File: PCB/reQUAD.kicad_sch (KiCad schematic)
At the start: 7 parts, among them J1 Model_100_System_BUS, U1 74LVC2G79, U2 74AC02, U4 74AC573, U5 628128

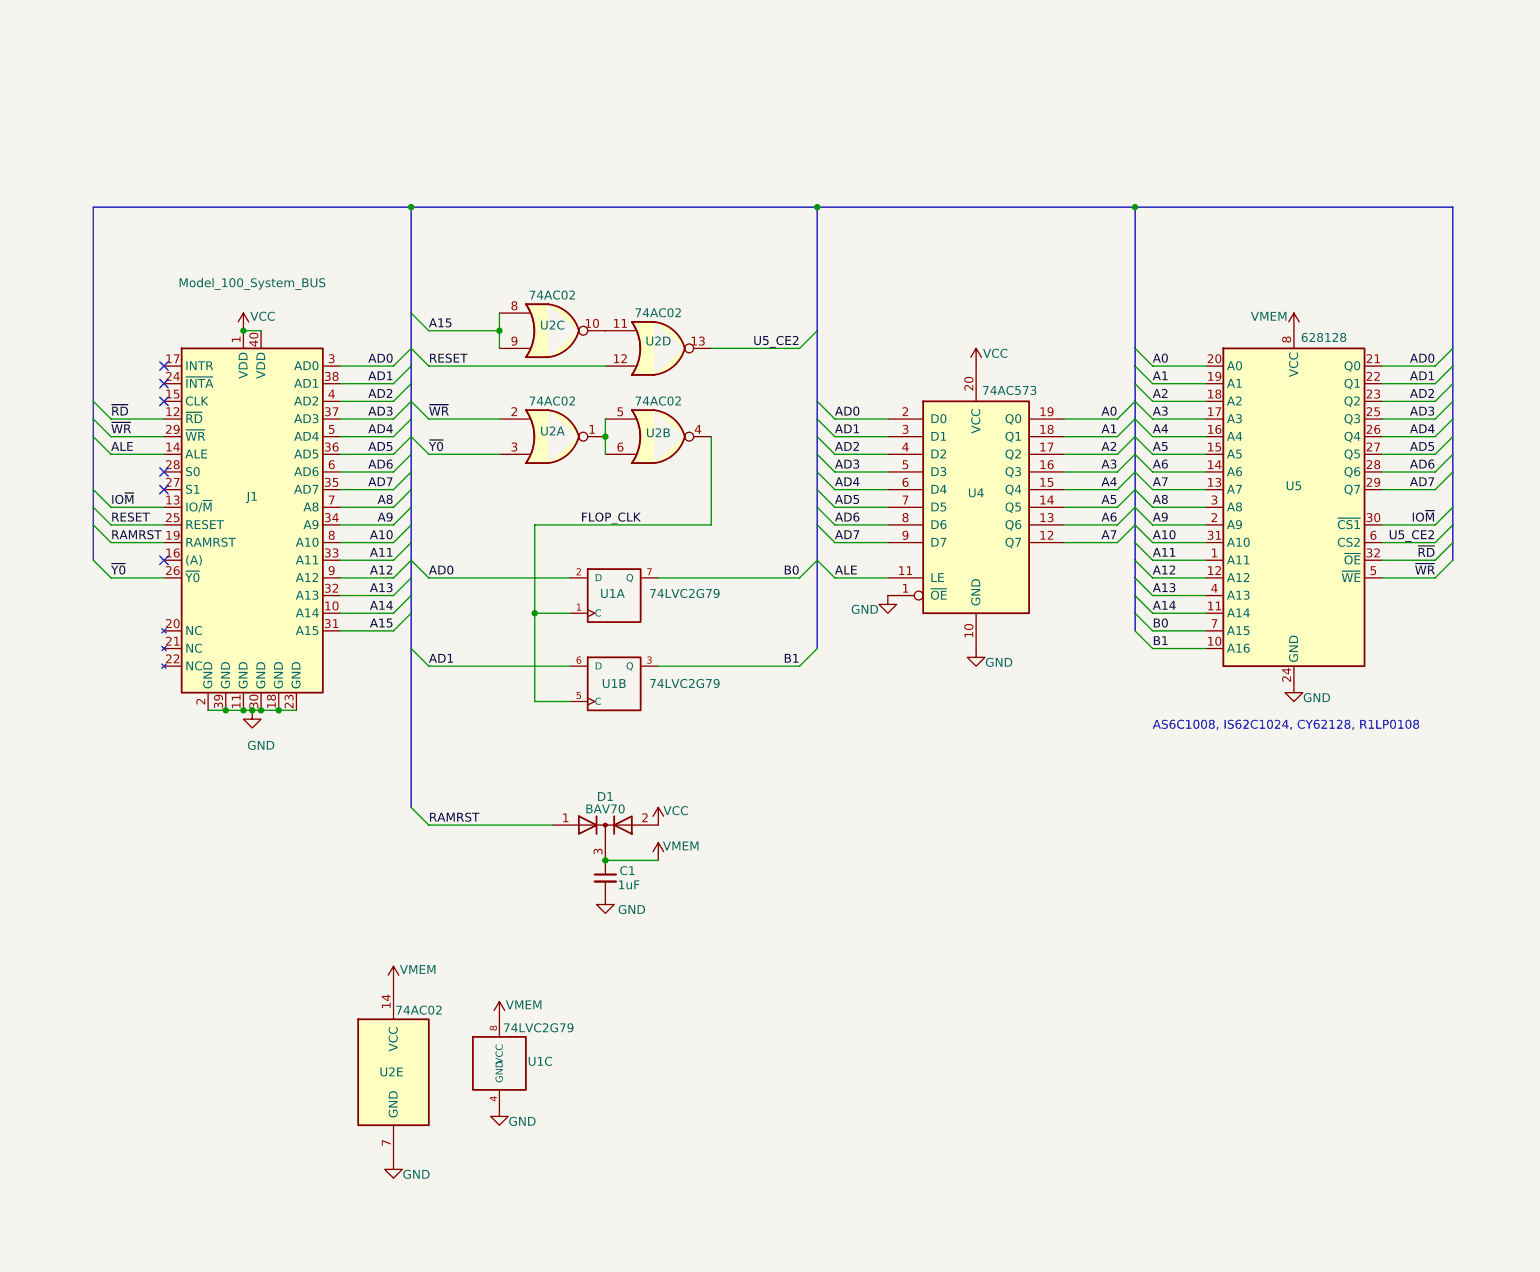
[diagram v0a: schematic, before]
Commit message: Try Steve's new idea: Pull (A)* low instead of pulling RAMRST high
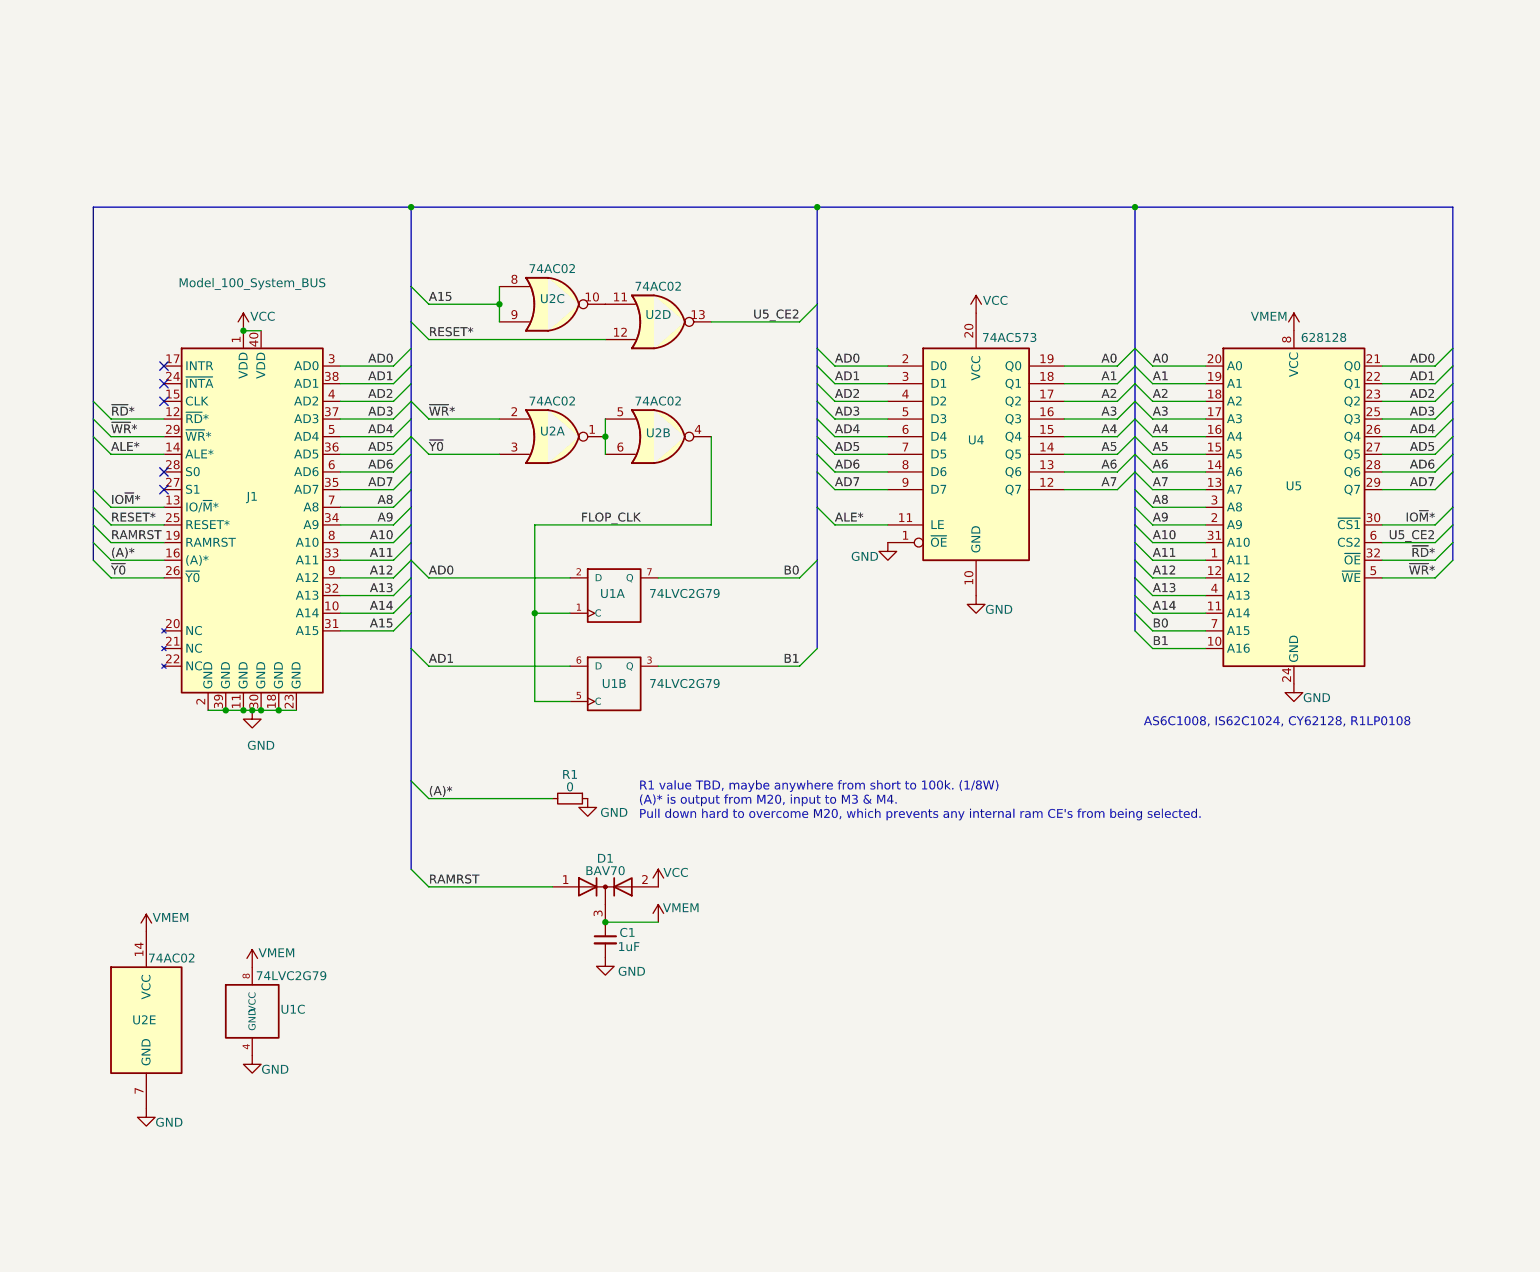
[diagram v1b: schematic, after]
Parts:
- added R1: 0, 000_LOCAL:R_0805, symbol 000_LOCAL:R_Small
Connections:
- net GND: now also R1.1
- net (A)*: now reaches J1.16 ((A)*)
- net (A)*: now also R1.2
- net ALE renamed ALE*
- net IO~{M} renamed IO~{M}*
- net RESET renamed RESET*
- net ~{RD} renamed ~{RD}*
- net ~{WR} renamed ~{WR}*
- no-connect marks 6 -> 5
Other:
- note added: "R1 value TBD, maybe anywhere from short to 100k. (1/8W) (A)* is output from M20, input to M3 & M4. Pull down hard to overcome M20, which prevents any internal ram CE's from being selected."
- moved on the sheet: C1, D1, U1C, U2C, U2D, U2E, U4

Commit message: pcb routing vcc vmem A0-A3
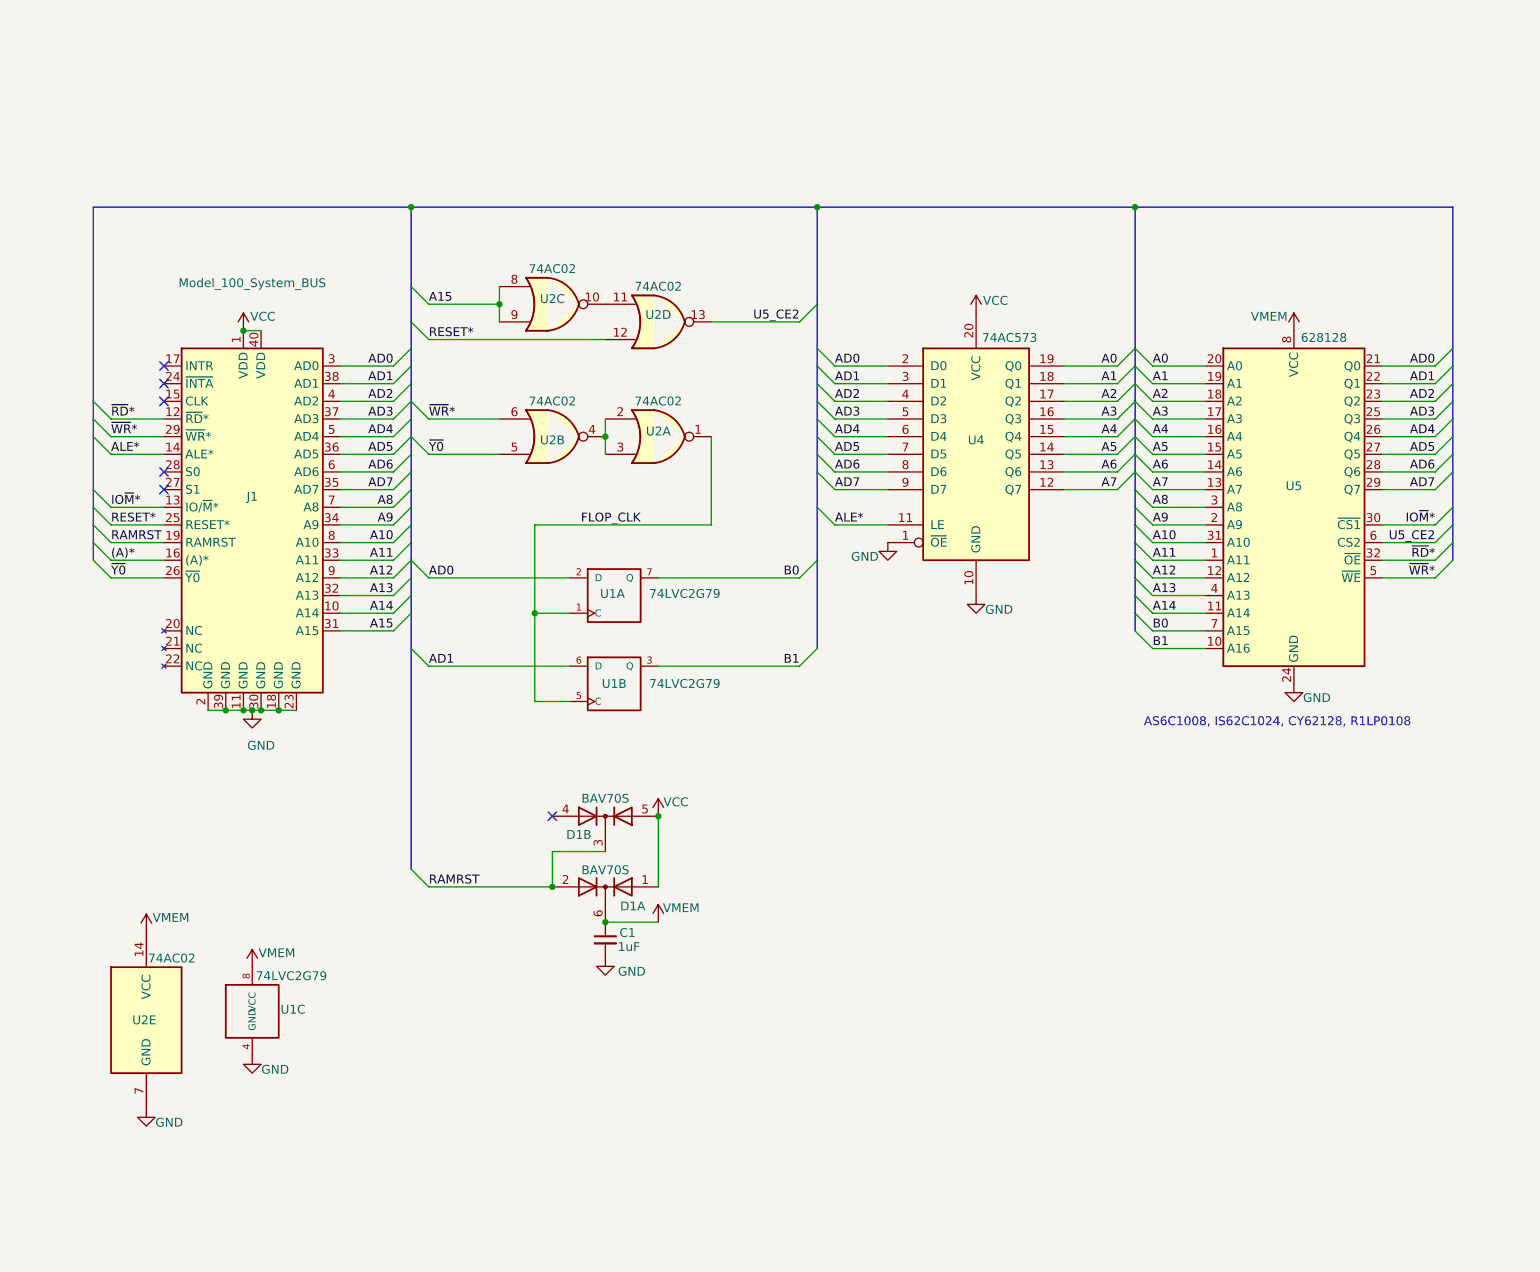
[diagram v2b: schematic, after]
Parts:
- removed D1: BAV70, 000_LOCAL:SOT-23, symbol 000_LOCAL:BAV70
- removed R1: 0, 000_LOCAL:R_0805, symbol 000_LOCAL:R_Small
- added D1: BAV70S, 000_LOCAL:SOT-363_symmetric, symbol 000_LOCAL:BAV70S
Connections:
- net FLOP_CLK: now also U2.1; no longer U2.4
- net RAMRST: now also D1.2 (A), D1.3 (K)
- net VCC: now also D1.1 (A), D1.5 (A)
- net VMEM: now also D1.6 (K)
- net ~{WR}*: now also U2.6; no longer U2.2
- net ~{Y0}: now also U2.5; no longer U2.3
- new net: U2.2, U2.3, U2.4
- no-connect marks 5 -> 6
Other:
- note removed: "R1 value TBD, maybe anywhere from short to 100k. (1/8W) (A)* is output from M20, input to M3 & M4. Pull down hard to overcome M20, which prevents any internal ram CE's from being selected."
- moved on the sheet: U2A, U2B

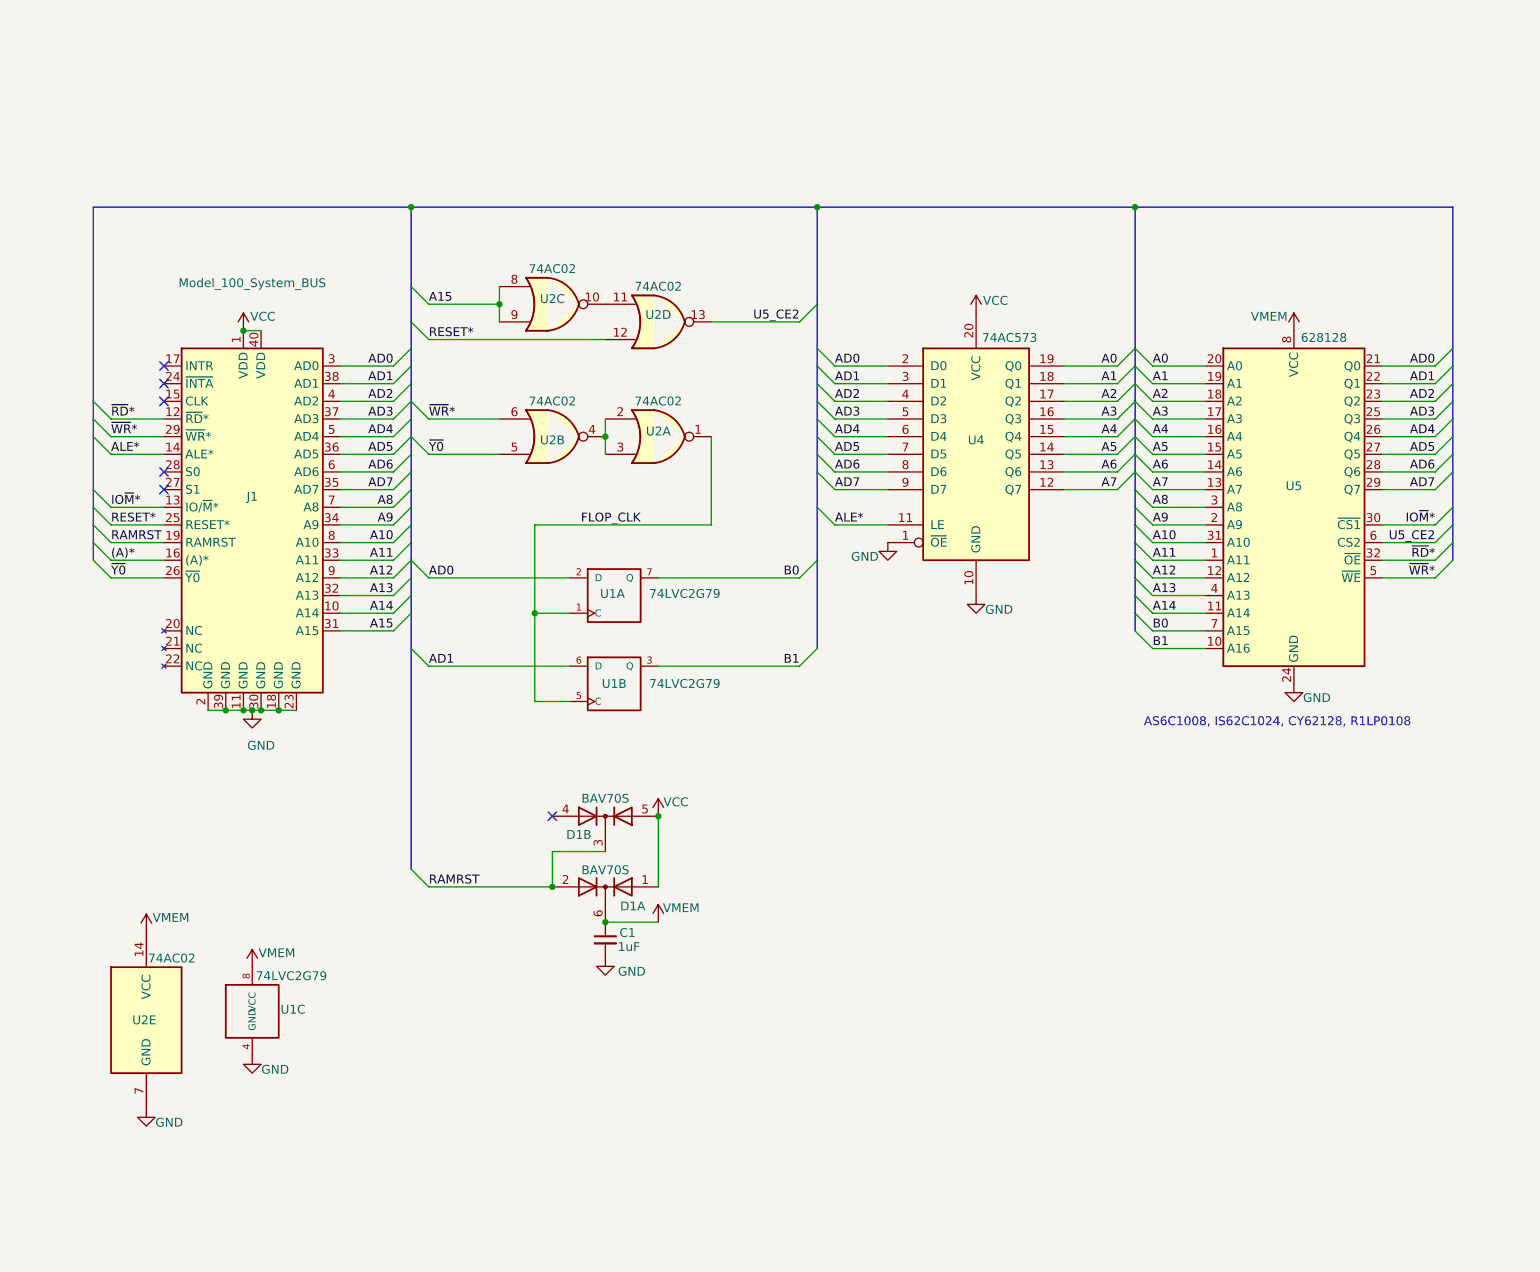
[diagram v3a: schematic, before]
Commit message: only need the flipflops on vmem?
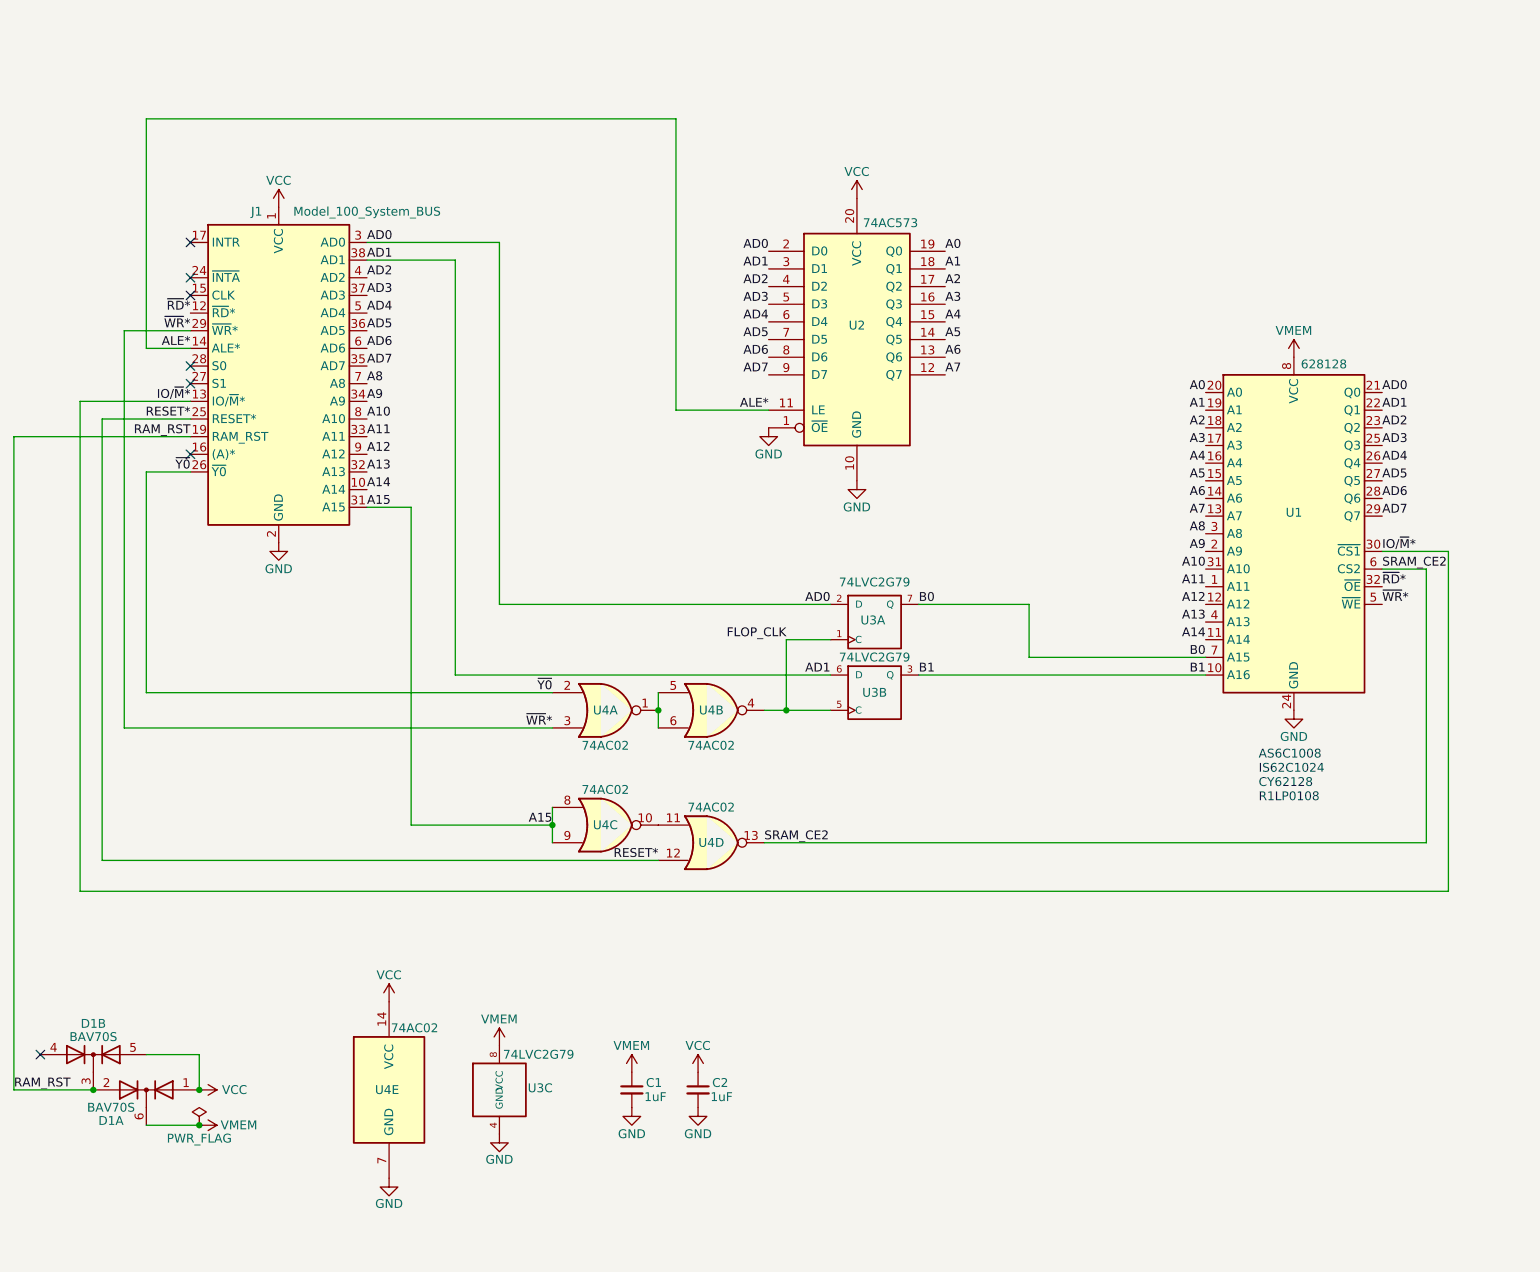
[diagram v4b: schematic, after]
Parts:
- added C2: 1uF, 000_LOCAL:C_0805, symbol 000_LOCAL:C_Small
- J1: footprint 000_LOCAL:DIP-40_pins -> Package_DIP:DIP-40_W15.24mm_Socket
- renumbered U5 to U1, U4 to U2, U1 to U3, U2 to U4
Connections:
- net FLOP_CLK: now also U4.4; no longer U4.1
- net GND: now also C2.2
- net VCC: now also U4.14 (VCC), C2.1
- net VMEM: no longer U4.14 (VCC)
- net ~{WR}*: now also U4.3; no longer U4.6
- net ~{Y0}: now also U4.2; no longer U4.5
- net (A)*: no longer names the net of J1.16 ((A)*)
- net IO~{M}* renamed IO/~{M}*
- net RAMRST renamed RAM_RST
- net U5_CE2 renamed SRAM_CE2
- new net: U4.1, U4.5, U4.6
- no-connect marks 6 -> 7
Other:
- note added: "AS6C1008 IS62C1024 CY62128 R1LP0108"
- note removed: "AS6C1008, IS62C1024, CY62128, R1LP0108"
- moved on the sheet: C1, D1A, D1B, U1, U2, U3A, U3B, U3C, U4A, U4B, U4C, U4D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

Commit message: add vcc cap
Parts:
- J1: footprint Package_DIP:DIP-40_W15.24mm_Socket -> 000_LOCAL:DIP-40_pins
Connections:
- net VCC: no longer U4.14 (VCC)
- net VMEM: now also U4.14 (VCC)
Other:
- moved on the sheet: J1, U1, U2
